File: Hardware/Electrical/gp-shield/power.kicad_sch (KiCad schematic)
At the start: 30 parts, among them J1 XT60/TERM2, J2 XT60/TERM2, Q1 Q_PMOS_GDS, SW1 SW_SPDT, U1 NCP1117-5.0_SOT223, U2 LM4040DBZ-2.5, U4 LM397

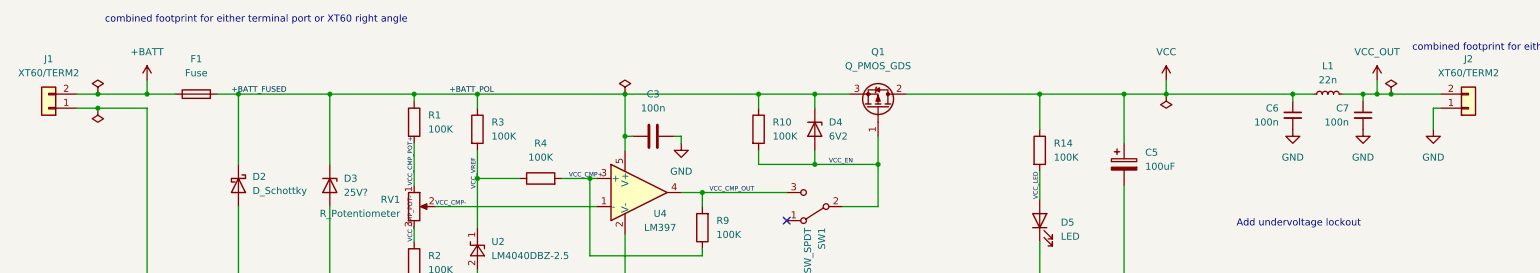
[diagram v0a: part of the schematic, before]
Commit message: Major PCB changes
Added combined footprint for XT60 and terminal port.
Fixed polarity of Batt and PWR_out connectors.
Standardised polarity markers to show negative on white.
Moved Port D and Port B connectors to be inline with existing arduino connectors. Removed extra pins.
Added analogue in-line output.
Adjusted component placement for more space around power supply and GP PB and LED.
Draft version of track routing - incomplete.
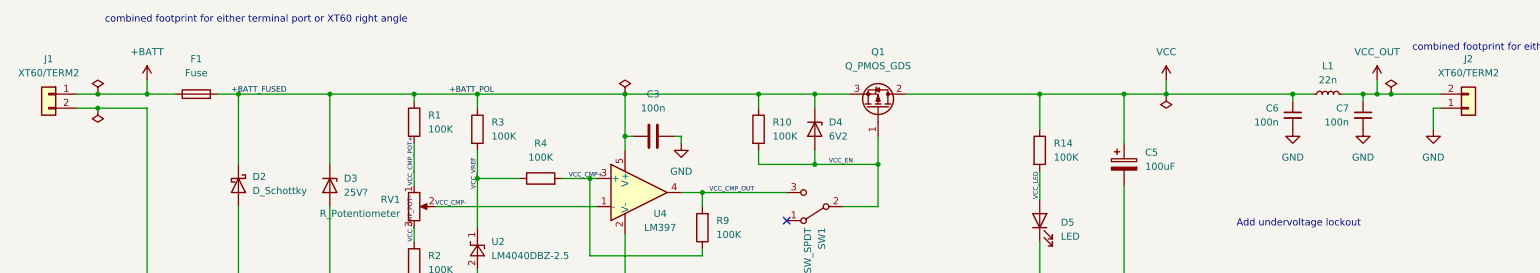
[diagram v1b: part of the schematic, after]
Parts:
- J1, J2: footprint TerminalBlock:TerminalBlock_bornier-2_P5.08mm -> Utility:Combined_TerminalBlock_5.08_XT60_2Row0.2Header
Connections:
- net +BATT: now also J1.1 (Pin_1); no longer J1.2 (Pin_2)
- net GND: now also J1.2 (Pin_2); no longer J1.1 (Pin_1)
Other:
- moved on the sheet: J1
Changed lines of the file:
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@@
   (junction (at 212.09 31.75) (diameter 0) (color 0 0 0 0)
   )
+  (junction (at 26.67 31.75) (diameter 0) (color 0 0 0 0)
+  )
   (junction (at 156.21 31.75) (diameter 0) (color 0 0 0 0)
   )
@@
   (junction (at 146.05 31.75) (diameter 0) (color 0 0 0 0)
   )
+  (junction (at 260.35 31.75) (diameter 0) (color 0 0 0 0)
+  )
   (junction (at 121.92 39.37) (diameter 0) (color 0 0 0 0)
   )
@@
   (junction (at 121.92 67.31) (diameter 0) (color 0 0 0 0)
   )
+  (junction (at 26.67 34.29) (diameter 0) (color 0 0 0 0)
+  )
   (junction (at 121.92 31.75) (diameter 0) (color 0 0 0 0)
   )
@@
   (junction (at 156.21 44.45) (diameter 0) (color 0 0 0 0)
   )
-  (junction (at 260.35 31.75) (diameter 0) (color 0 0 0 0)
-  )
-  (junction (at 26.67 34.29) (diameter 0) (color 0 0 0 0)
-  )
   (junction (at 257.81 31.75) (diameter 0) (color 0 0 0 0)
   )
@@
   )
   (junction (at 115.57 46.99) (diameter 0) (color 0 0 0 0)
-  )
-  (junction (at 26.67 31.75) (diameter 0) (color 0 0 0 0)
   )
   (no_connect (at 151.13 54.61))
@@
     (stroke (width 0) (type default) (color 0 0 0 0))
   )
+  (wire (pts (xy 22.86 31.75) (xy 26.67 31.75))
+    (stroke (width 0) (type default) (color 0 0 0 0))
+  )
   (wire (pts (xy 35.56 67.31) (xy 52.07 67.31))
     (stroke (width 0) (type default) (color 0 0 0 0))
@@
     (stroke (width 0) (type default) (color 0 0 0 0))
   )
+  (wire (pts (xy 22.86 34.29) (xy 26.67 34.29))
+    (stroke (width 0) (type default) (color 0 0 0 0))
+  )
   (wire (pts (xy 161.29 52.07) (xy 167.64 52.07))
     (stroke (width 0) (type default) (color 0 0 0 0))
@@
     (stroke (width 0) (type default) (color 0 0 0 0))
   )
+  (wire (pts (xy 105.41 119.38) (xy 105.41 125.73))
+    (stroke (width 0) (type default) (color 0 0 0 0))
+  )
+  (wire (pts (xy 35.56 67.31) (xy 35.56 34.29))
+    (stroke (width 0) (type default) (color 0 0 0 0))
+  )
+  (wire (pts (xy 196.85 45.72) (xy 196.85 50.8))
+    (stroke (width 0) (type default) (color 0 0 0 0))
+  )
+  (wire (pts (xy 219.71 29.21) (xy 219.71 31.75))
+    (stroke (width 0) (type default) (color 0 0 0 0))
+  )
   (wire (pts (xy 260.35 31.75) (xy 269.24 31.75))
     (stroke (width 0) (type default) (color 0 0 0 0))
   )
-  (wire (pts (xy 105.41 119.38) (xy 105.41 125.73))
-    (stroke (width 0) (type default) (color 0 0 0 0))
-  )
-  (wire (pts (xy 35.56 67.31) (xy 35.56 34.29))
-    (stroke (width 0) (type default) (color 0 0 0 0))
-  )
-  (wire (pts (xy 196.85 45.72) (xy 196.85 50.8))
-    (stroke (width 0) (type default) (color 0 0 0 0))
-  )
-  (wire (pts (xy 219.71 29.21) (xy 219.71 31.75))
-    (stroke (width 0) (type default) (color 0 0 0 0))
-  )
   (wire (pts (xy 35.56 67.31) (xy 35.56 69.85))
     (stroke (width 0) (type default) (color 0 0 0 0))
@@
     (stroke (width 0) (type default) (color 0 0 0 0))
   )
-  (wire (pts (xy 269.24 34.29) (xy 267.97 34.29))
-    (stroke (width 0) (type default) (color 0 0 0 0))
-  )
   (wire (pts (xy 121.92 57.15) (xy 121.92 67.31))
     (stroke (width 0) (type default) (color 0 0 0 0))
@@
     (stroke (width 0) (type default) (color 0 0 0 0))
   )
+  (wire (pts (xy 267.97 34.29) (xy 269.24 34.29))
+    (stroke (width 0) (type default) (color 0 0 0 0))
+  )
   (wire (pts (xy 78.74 116.84) (xy 78.74 121.92))
     (stroke (width 0) (type default) (color 0 0 0 0))
@@
     (stroke (width 0) (type default) (color 0 0 0 0))
   )
-  (wire (pts (xy 26.67 34.29) (xy 22.86 34.29))
-    (stroke (width 0) (type default) (color 0 0 0 0))
-  )
   (wire (pts (xy 135.89 49.53) (xy 151.13 49.53))
     (stroke (width 0) (type default) (color 0 0 0 0))
@@
   )
   (wire (pts (xy 68.58 52.07) (xy 68.58 67.31))
-    (stroke (width 0) (type default) (color 0 0 0 0))
-  )
-  (wire (pts (xy 22.86 31.75) (xy 26.67 31.75))
     (stroke (width 0) (type default) (color 0 0 0 0))
   )
@@
     (pin "1")
   )
-  (symbol (lib_id "Connector_Generic:Conn_01x02") (at 17.78 34.29 180) (unit 1)
+  (symbol (lib_id "Connector_Generic:Conn_01x02") (at 17.78 31.75 0) (mirror y) (unit 1)
     (in_bom yes) (on_board yes) (fields_autoplaced)
     (property "Reference" "J1" (id 0) (at 17.78 25.4 0))
     (property "Value" "XT60/TERM2" (id 1) (at 17.78 27.94 0))
-    (property "Footprint" "TerminalBlock:TerminalBlock_bornier-2_P5.08mm" (id 2) (at 17.78 34.29 0)
-      (effects (font (size 1.27 1.27)) hide)
-    )
-    (property "Datasheet" "~" (id 3) (at 17.78 34.29 0)
+    (property "Footprint" "Utility:Combined_TerminalBlock_5.08_XT60_2Row0.2Header" (id 2) (at 17.78 31.75 0)
+      (effects (font (size 1.27 1.27)) hide)
+    )
+    (property "Datasheet" "~" (id 3) (at 17.78 31.75 0)
       (effects (font (size 1.27 1.27)) hide)
     )
@@
     (property "Reference" "J2" (id 0) (at 274.32 25.4 0))
     (property "Value" "XT60/TERM2" (id 1) (at 274.32 27.94 0))
-    (property "Footprint" "TerminalBlock:TerminalBlock_bornier-2_P5.08mm" (id 2) (at 274.32 34.29 0)
-      (effects (font (size 1.27 1.27)) hide)
-    )
+    (property "Footprint" "Utility:Combined_TerminalBlock_5.08_XT60_2Row0.2Header" (id 2) (at 274.32 34.29 0)
+      (effects (font (size 1.27 1.27)) hide)
+    )

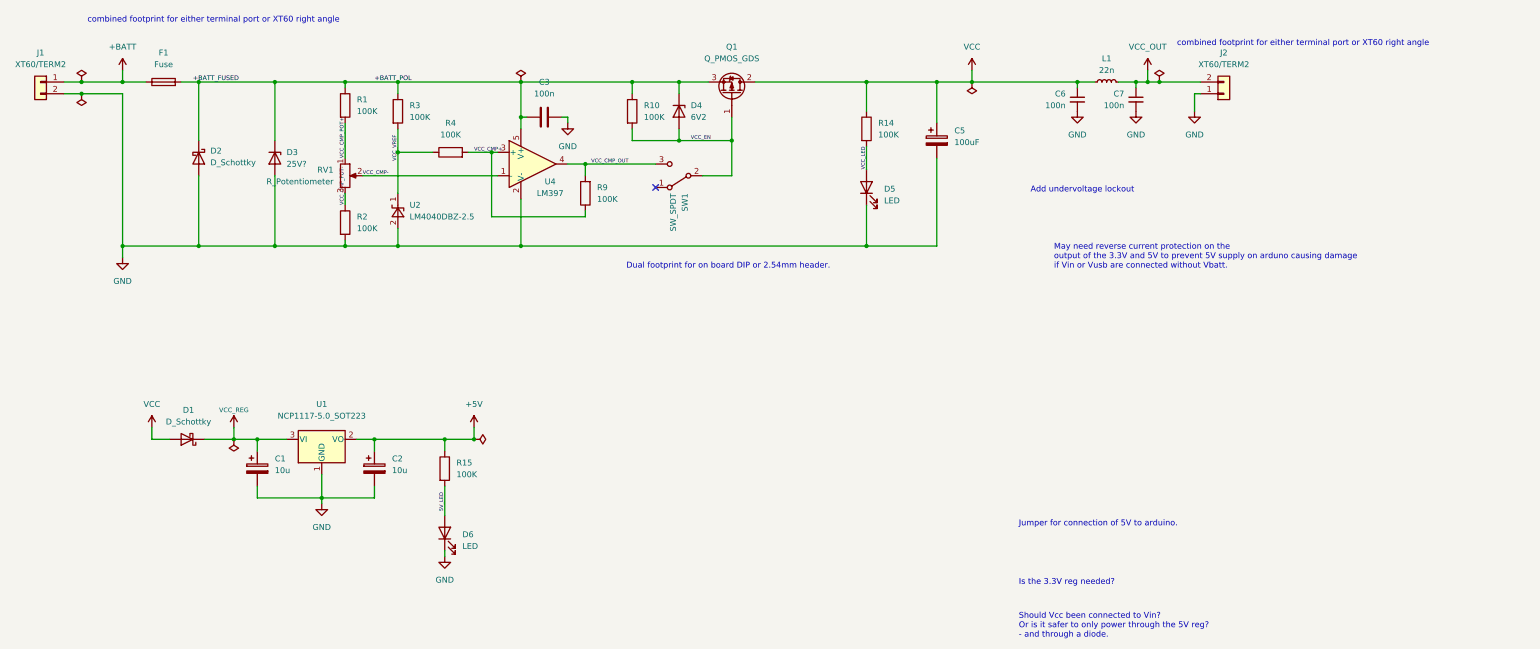
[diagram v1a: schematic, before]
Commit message: Complete draft PCB layout
Added updated renders to doc.
Added some documentation to schematic
complete PCB layout with some revisions still needed
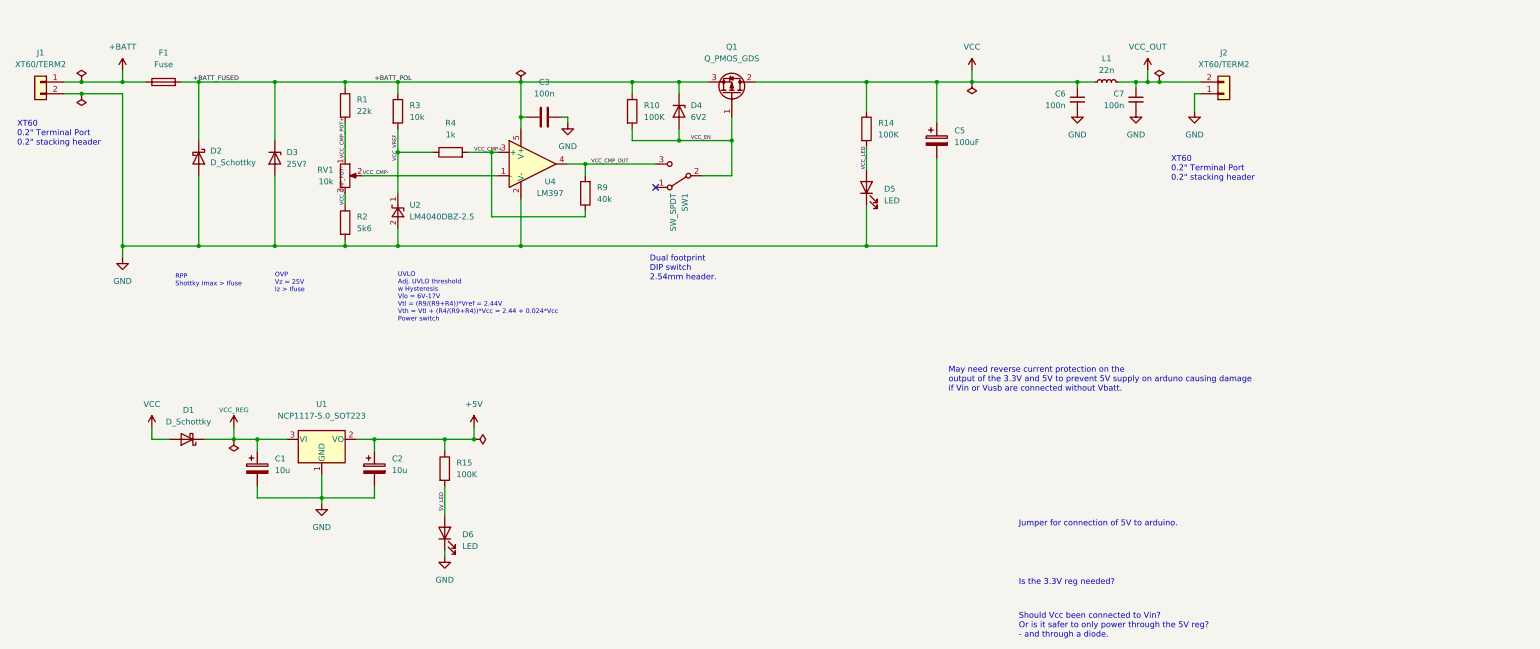
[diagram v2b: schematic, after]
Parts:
- R1: value 100K -> 22k
- R2: value 100K -> 5k6
- R3: value 100K -> 10k
- R4: value 100K -> 1k
- R9: value 100K -> 40k
- RV1: value R_Potentiometer -> 10k
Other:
- note added: "Dual footprint DIP switch 2.54mm header."
- note added: "OVP Vz = 25V Iz > Ifuse"
- note added: "RPP Shottky Imax > Ifuse"
- note added: "UVLO Adj. UVLO threshold w Hysteresis Vlo = 6V-17V Vtl = (R9/(R9+R4))*Vref = 2.44V Vth = Vtl + (R4/(R9+R4))*Vcc = 2.44 + 0.024*Vcc Power switch"
- note added: "XT60 0.2" Terminal Port 0.2" stacking header"
- note removed: "Add undervoltage lockout"
- note removed: "Dual footprint for on board DIP or 2.54mm header."
- note removed: "combined footprint for either terminal port or XT60 right angle"
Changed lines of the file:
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@@
     (stroke (width 0) (type default) (color 0 0 0 0))
   )
-  (text "combined footprint for either terminal port or XT60 right angle"
-    (at 27.94 19.05 0)
+  (text "OVP\nVz = 25V\nIz > Ifuse" (at 68.58 77.47 0)
+    (effects (font (size 1 1)) (justify left bottom))
+  )
+  (text "XT60\n0.2\" Terminal Port\n0.2\" stacking header" (at 12.7 45.72 0)
     (effects (font (size 1.27 1.27)) (justify left bottom))
   )
@@
     (effects (font (size 1.27 1.27)) (justify left bottom))
   )
-  (text "Dual footprint for on board DIP or 2.54mm header." (at 144.78 72.39 0)
+  (text "Dual footprint\nDIP switch\n2.54mm header." (at 149.86 74.93 0)
+    (effects (font (size 1.27 1.27)) (justify left bottom))
+  )
+  (text "XT60\n0.2\" Terminal Port\n0.2\" stacking header" (at 262.89 53.34 0)
     (effects (font (size 1.27 1.27)) (justify left bottom))
   )
@@
     (effects (font (size 1.27 1.27)) (justify left bottom))
   )
+  (text "UVLO\nAdj. UVLO threshold\nw Hysteresis\nVlo = 6V-17V\nVtl = (R9/(R9+R4))*Vref = 2.44V\nVth = Vtl + (R4/(R9+R4))*Vcc = 2.44 + 0.024*Vcc\nPower switch"
+    (at 95.25 83.82 0)
+    (effects (font (size 1 1)) (justify left bottom))
+  )
   (text "May need reverse current protection on the\noutput of the 3.3V and 5V to prevent 5V supply on arduno causing damage\nif Vin or Vusb are connected without Vbatt."
-    (at 237.49 72.39 0)
+    (at 214.63 99.06 0)
     (effects (font (size 1.27 1.27)) (justify left bottom))
   )
@@
     (effects (font (size 1.27 1.27)) (justify left bottom))
   )
-  (text "combined footprint for either terminal port or XT60 right angle"
-    (at 264.16 24.13 0)
-    (effects (font (size 1.27 1.27)) (justify left bottom))
-  )
-  (text "Add undervoltage lockout" (at 232.41 55.88 0)
-    (effects (font (size 1.27 1.27)) (justify left bottom))
+  (text "RPP\nShottky Imax > Ifuse" (at 46.99 76.2 0)
+    (effects (font (size 1 1)) (justify left bottom))
   )
   (label "VCC_LED" (at 196.85 45.72 270)
@@
       (effects (font (size 1.27 1.27)) (justify right))
     )
-    (property "Value" "100K" (id 1) (at 138.43 57.1499 0)
+    (property "Value" "40k" (id 1) (at 138.43 57.1499 0)
       (effects (font (size 1.27 1.27)) (justify right))
     )
@@
       (effects (font (size 1.27 1.27)) (justify left))
     )
-    (property "Value" "100K" (id 1) (at 86.36 38.0999 0)
+    (property "Value" "22k" (id 1) (at 86.36 38.0999 0)
       (effects (font (size 1.27 1.27)) (justify left))
     )
@@
       (effects (font (size 1.27 1.27)) (justify left))
     )
-    (property "Value" "100K" (id 1) (at 86.36 63.4999 0)
+    (property "Value" "5k6" (id 1) (at 86.36 63.4999 0)
       (effects (font (size 1.27 1.27)) (justify left))
     )
@@
       (effects (font (size 1.27 1.27)) (justify left))
     )
-    (property "Value" "100K" (id 1) (at 97.79 39.3699 0)
+    (property "Value" "10k" (id 1) (at 97.79 39.3699 0)
       (effects (font (size 1.27 1.27)) (justify left))
     )
@@
       (effects (font (size 1.27 1.27)) (justify right))
     )
-    (property "Value" "R_Potentiometer" (id 1) (at 81.28 53.3399 0)
+    (property "Value" "10k" (id 1) (at 81.28 53.3399 0)
       (effects (font (size 1.27 1.27)) (justify right))
     )
@@
     (in_bom yes) (on_board yes) (fields_autoplaced)
     (property "Reference" "R4" (id 0) (at 106.68 40.64 90))
-    (property "Value" "100K" (id 1) (at 106.68 43.18 90))
+    (property "Value" "1k" (id 1) (at 106.68 43.18 90))
     (property "Footprint" "Resistor_SMD:R_0805_2012Metric_Pad1.20x1.40mm_HandSolder" (id 2) (at 106.68 48.768 90)
       (effects (font (size 1.27 1.27)) hide)
